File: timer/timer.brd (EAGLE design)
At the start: 100 x 80 mm, 8 parts, among them IC1 LM555N

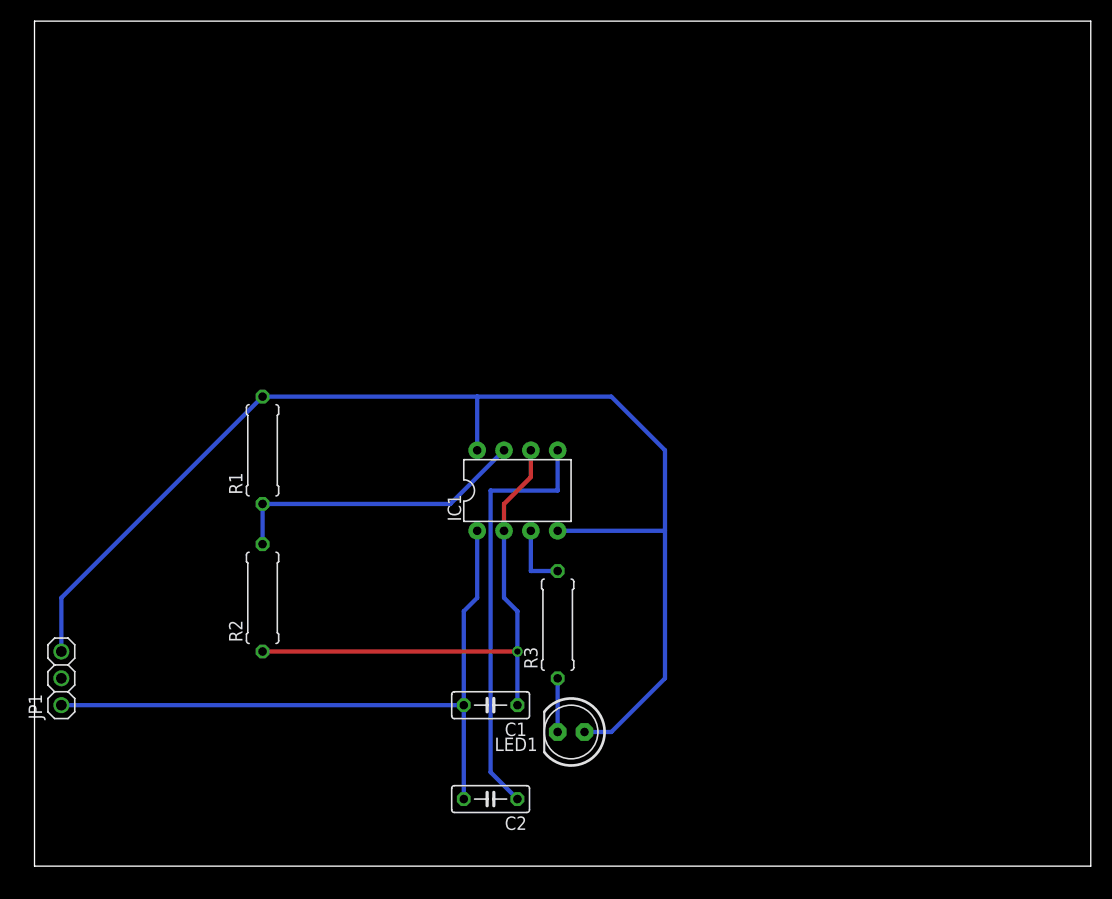
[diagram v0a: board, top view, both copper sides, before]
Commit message: add mounting holes
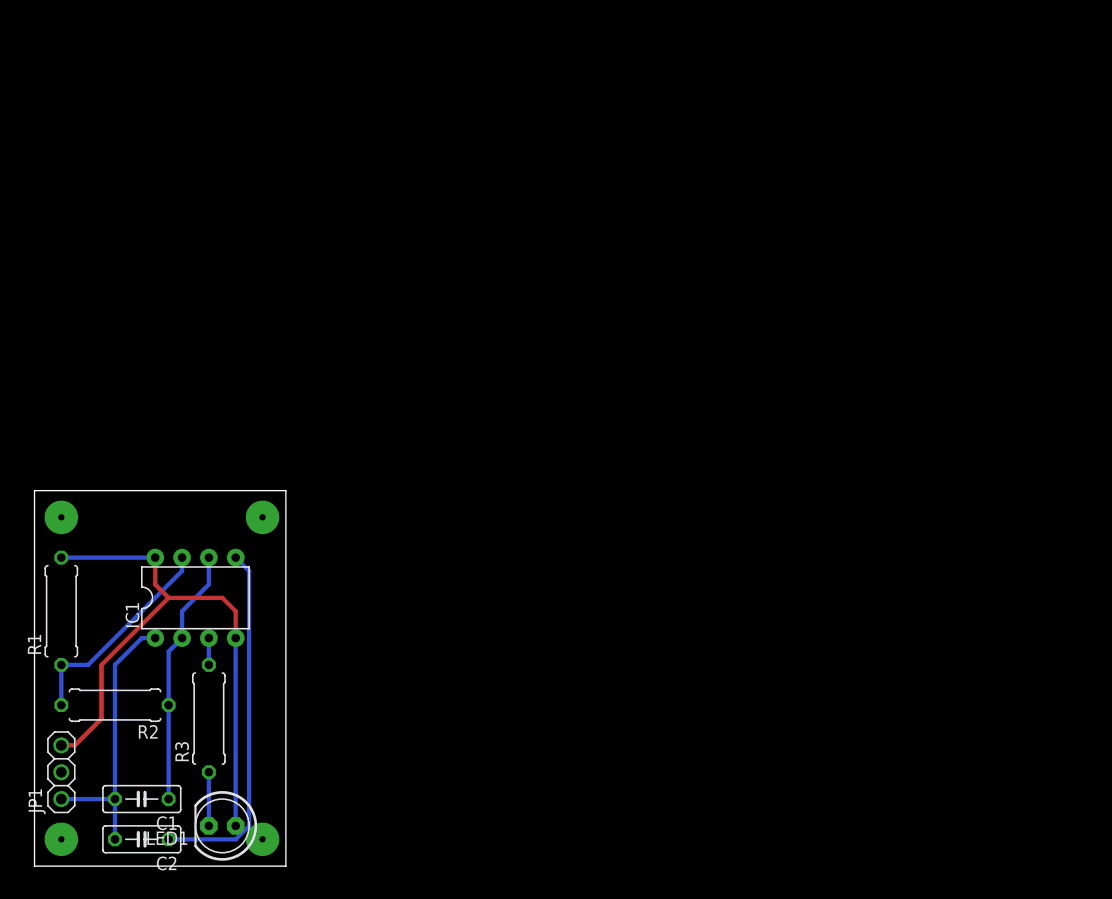
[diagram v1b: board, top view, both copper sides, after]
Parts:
- moved C1 34.2 mm to (10.2, 6.35)
- moved LED1 34.2 mm to (17.8, 3.81)
- moved R3 34.2 mm to (16.5, 14.0)
- moved C2 33.2 mm to (10.2, 2.54)
- moved IC1 32.1 mm to (15.2, 25.4)
- moved R1 24.4 mm to (2.54, 24.1)
- moved R2 17.3 mm to (7.62, 15.2), turned to 180 degrees
- moved JP1 8.89 mm to (2.54, 8.89)
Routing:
- net N$7: track 118.8 -> 59.3 mm
- net N$5: track 64.0 -> 26.5 mm
- net N$9: track 49.8 -> 24.4 mm, vias 1 -> 0
- net N$3: track 28.8 -> 20.2 mm
- net N$1: track 40.4 -> 34.1 mm
- net N$4: track 6.35 -> 2.54 mm
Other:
- board size 100 x 80 mm -> 23.8 x 35.5 mm
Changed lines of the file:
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@@
 <?xml version="1.0" encoding="utf-8"?>
 <!DOCTYPE eagle SYSTEM "eagle.dtd">
-<eagle version="6.2">
+<eagle version="6.3">
 <drawing>
 <settings>
@@
 <board>
 <plain>
-<wire x1="0" y1="0" x2="100" y2="0" width="0" layer="20"/>
-<wire x1="100" y1="0" x2="100" y2="80" width="0" layer="20"/>
-<wire x1="100" y1="80" x2="0" y2="80" width="0" layer="20"/>
-<wire x1="0" y1="80" x2="0" y2="0" width="0" layer="20"/>
+<wire x1="0" y1="0" x2="23.8" y2="0" width="0" layer="20"/>
+<wire x1="23.8" y1="0" x2="23.8" y2="35.55" width="0" layer="20"/>
+<wire x1="23.8" y1="35.55" x2="0" y2="35.55" width="0" layer="20"/>
+<wire x1="0" y1="35.55" x2="0" y2="0" width="0" layer="20"/>
 </plain>
 <attributes>
@@
 </class>
 </classes>
-<designrules>
+<designrules name="default">
 <description language="de">&lt;b&gt;EAGLE Design Rules&lt;/b&gt;
 &lt;p&gt;
@@
 </autorouter>
 <elements>
-<element name="IC1" library="adafruit" package="DIL08-ROUND" value="LM555N" x="45.72" y="35.56"/>
-<element name="R1" library="adafruit" package="0309/10" value="10k" x="21.59" y="39.37" rot="R90"/>
-<element name="R2" library="adafruit" package="0309/10" value="220k" x="21.59" y="25.4" rot="R90"/>
-<element name="R3" library="adafruit" package="0309/10" value="470" x="49.53" y="22.86" rot="R90"/>
-<element name="C2" library="adafruit" package="C050-025X075" value="0.1uf" x="43.18" y="6.35" rot="R180"/>
-<element name="C1" library="adafruit" package="C050-025X075" value="1uf" x="43.18" y="15.24" rot="R180"/>
-<element name="LED1" library="adafruit" package="LED5MM" value="" x="50.8" y="12.7" rot="R180"/>
-<element name="JP1" library="adafruit" package="1X03" value="" x="2.54" y="17.78" rot="R90"/>
+<element name="IC1" library="adafruit" package="DIL08-ROUND" value="LM555N" x="15.24" y="25.4"/>
+<element name="R1" library="adafruit" package="0309/10" value="10k" x="2.54" y="24.13" rot="R90"/>
+<element name="R2" library="adafruit" package="0309/10" value="220k" x="7.62" y="15.24" rot="R180"/>
+<element name="R3" library="adafruit" package="0309/10" value="470" x="16.51" y="13.97" rot="R90"/>
+<element name="C2" library="adafruit" package="C050-025X075" value="0.1uf" x="10.16" y="2.54" rot="R180"/>
+<element name="C1" library="adafruit" package="C050-025X075" value="1uf" x="10.16" y="6.35" rot="R180"/>
+<element name="LED1" library="adafruit" package="LED5MM" value="" x="17.78" y="3.81" rot="R180"/>
+<element name="JP1" library="adafruit" package="1X03" value="" x="2.54" y="8.89" rot="R90"/>
 </elements>
 <signals>
@@
 <contactref element="R2" pad="2"/>
 <contactref element="IC1" pad="7"/>
-<wire x1="21.59" y1="34.29" x2="21.59" y2="30.48" width="0.4064" layer="16"/>
-<wire x1="44.45" y1="39.37" x2="39.37" y2="34.29" width="0.4064" layer="16"/>
-<wire x1="39.37" y1="34.29" x2="21.59" y2="34.29" width="0.4064" layer="16"/>
+<wire x1="2.54" y1="19.05" x2="2.54" y2="15.24" width="0.4064" layer="16"/>
+<wire x1="13.97" y1="29.21" x2="13.97" y2="27.94" width="0.4064" layer="16"/>
+<wire x1="13.97" y1="27.94" x2="5.08" y2="19.05" width="0.4064" layer="16"/>
+<wire x1="5.08" y1="19.05" x2="2.54" y2="19.05" width="0.4064" layer="16"/>
 </signal>
 <signal name="N$5">
@@
 <contactref element="IC1" pad="1"/>
 <contactref element="C2" pad="2"/>
-<wire x1="40.64" y1="6.35" x2="40.64" y2="15.24" width="0.4064" layer="16"/>
-<wire x1="40.64" y1="15.24" x2="40.64" y2="24.13" width="0.4064" layer="16"/>
-<wire x1="40.64" y1="24.13" x2="41.91" y2="25.4" width="0.4064" layer="16"/>
-<wire x1="41.91" y1="25.4" x2="41.91" y2="31.75" width="0.4064" layer="16"/>
-<wire x1="2.54" y1="15.24" x2="40.64" y2="15.24" width="0.4064" layer="16"/>
+<wire x1="7.62" y1="2.54" x2="7.62" y2="6.35" width="0.4064" layer="16"/>
+<wire x1="2.54" y1="6.35" x2="7.62" y2="6.35" width="0.4064" layer="16"/>
+<wire x1="11.43" y1="21.59" x2="10.16" y2="21.59" width="0.4064" layer="16"/>
+<wire x1="10.16" y1="21.59" x2="7.62" y2="19.05" width="0.4064" layer="16"/>
+<wire x1="7.62" y1="19.05" x2="7.62" y2="6.35" width="0.4064" layer="16"/>
 </signal>
 <signal name="N$7">
@@
 <contactref element="IC1" pad="4"/>
 <contactref element="LED1" pad="A"/>
-<wire x1="21.59" y1="44.45" x2="41.91" y2="44.45" width="0.4064" layer="16"/>
-<wire x1="41.91" y1="44.45" x2="41.91" y2="39.37" width="0.4064" layer="16"/>
-<wire x1="54.61" y1="44.45" x2="41.91" y2="44.45" width="0.4064" layer="16"/>
-<wire x1="54.61" y1="44.45" x2="59.69" y2="39.37" width="0.4064" layer="16"/>
-<wire x1="59.69" y1="39.37" x2="59.69" y2="31.75" width="0.4064" layer="16"/>
-<wire x1="59.69" y1="31.75" x2="49.53" y2="31.75" width="0.4064" layer="16"/>
-<wire x1="52.07" y1="12.7" x2="54.61" y2="12.7" width="0.4064" layer="16"/>
-<wire x1="54.61" y1="12.7" x2="59.69" y2="17.78" width="0.4064" layer="16"/>
-<wire x1="59.69" y1="17.78" x2="59.69" y2="31.75" width="0.4064" layer="16"/>
-<wire x1="2.54" y1="20.32" x2="2.54" y2="25.4" width="0.4064" layer="16"/>
-<wire x1="2.54" y1="25.4" x2="21.59" y2="44.45" width="0.4064" layer="16"/>
+<wire x1="11.43" y1="29.21" x2="2.54" y2="29.21" width="0.4064" layer="16"/>
+<wire x1="11.43" y1="29.21" x2="11.43" y2="26.67" width="0.4064" layer="1"/>
+<wire x1="11.43" y1="26.67" x2="12.7" y2="25.4" width="0.4064" layer="1"/>
+<wire x1="12.7" y1="25.4" x2="17.78" y2="25.4" width="0.4064" layer="1"/>
+<wire x1="17.78" y1="25.4" x2="19.05" y2="24.13" width="0.4064" layer="1"/>
+<wire x1="19.05" y1="24.13" x2="19.05" y2="21.59" width="0.4064" layer="1"/>
+<wire x1="19.05" y1="3.81" x2="19.05" y2="21.59" width="0.4064" layer="16"/>
+<wire x1="2.54" y1="11.43" x2="3.81" y2="11.43" width="0.4064" layer="1"/>
+<wire x1="3.81" y1="11.43" x2="6.35" y2="13.97" width="0.4064" layer="1"/>
+<wire x1="6.35" y1="13.97" x2="6.35" y2="19.05" width="0.4064" layer="1"/>
+<wire x1="6.35" y1="19.05" x2="12.7" y2="25.4" width="0.4064" layer="1"/>
 </signal>
 <signal name="N$9">
@@
 <contactref element="IC1" pad="2"/>
 <contactref element="IC1" pad="6"/>
-<wire x1="45.72" y1="15.24" x2="45.72" y2="20.32" width="0.4064" layer="16"/>
-<wire x1="45.72" y1="20.32" x2="45.72" y2="24.13" width="0.4064" layer="16"/>
-<wire x1="45.72" y1="24.13" x2="44.45" y2="25.4" width="0.4064" layer="16"/>
-<wire x1="44.45" y1="25.4" x2="44.45" y2="31.75" width="0.4064" layer="16"/>
-<wire x1="21.59" y1="20.32" x2="45.72" y2="20.32" width="0.4064" layer="1"/>
-<via x="45.72" y="20.32" extent="1-16" drill="0.6" shape="square"/>
-<wire x1="44.45" y1="31.75" x2="44.45" y2="34.29" width="0.4064" layer="1"/>
-<wire x1="44.45" y1="34.29" x2="46.99" y2="36.83" width="0.4064" layer="1"/>
-<wire x1="46.99" y1="36.83" x2="46.99" y2="39.37" width="0.4064" layer="1"/>
+<wire x1="12.7" y1="15.24" x2="12.7" y2="6.35" width="0.4064" layer="16"/>
+<wire x1="13.97" y1="21.59" x2="12.7" y2="20.32" width="0.4064" layer="16"/>
+<wire x1="12.7" y1="20.32" x2="12.7" y2="15.24" width="0.4064" layer="16"/>
+<wire x1="16.51" y1="29.21" x2="16.51" y2="26.67" width="0.4064" layer="16"/>
+<wire x1="16.51" y1="26.67" x2="13.97" y2="24.13" width="0.4064" layer="16"/>
+<wire x1="13.97" y1="24.13" x2="13.97" y2="21.59" width="0.4064" layer="16"/>
 </signal>
 <signal name="N$1">
 <contactref element="IC1" pad="5"/>
 <contactref element="C2" pad="1"/>
-<wire x1="49.53" y1="39.37" x2="49.53" y2="35.56" width="0.4064" layer="16"/>
-<wire x1="49.53" y1="35.56" x2="43.18" y2="35.56" width="0.4064" layer="16"/>
-<wire x1="43.18" y1="35.56" x2="43.18" y2="8.89" width="0.4064" layer="16"/>
-<wire x1="43.18" y1="8.89" x2="45.72" y2="6.35" width="0.4064" layer="16"/>
+<wire x1="19.05" y1="29.21" x2="20.32" y2="27.94" width="0.4064" layer="16"/>
+<wire x1="20.32" y1="27.94" x2="20.32" y2="3.81" width="0.4064" layer="16"/>
+<wire x1="20.32" y1="3.81" x2="19.05" y2="2.54" width="0.4064" layer="16"/>
+<wire x1="19.05" y1="2.54" x2="12.7" y2="2.54" width="0.4064" layer="16"/>
 </signal>
 <signal name="N$2">
 <contactref element="LED1" pad="K"/>
 <contactref element="R3" pad="1"/>
-<wire x1="49.53" y1="12.7" x2="49.53" y2="17.78" width="0.4064" layer="16"/>
+<wire x1="16.51" y1="8.89" x2="16.51" y2="3.81" width="0.4064" layer="16"/>
 </signal>
 <signal name="N$4">
 <contactref element="R3" pad="2"/>
 <contactref element="IC1" pad="3"/>
-<wire x1="49.53" y1="27.94" x2="46.99" y2="27.94" width="0.4064" layer="16"/>
-<wire x1="46.99" y1="27.94" x2="46.99" y2="31.75" width="0.4064" layer="16"/>
+<wire x1="16.51" y1="21.59" x2="16.51" y2="19.05" width="0.4064" layer="16"/>
+</signal>
+<signal name="N$6">
+<via x="2.54" y="2.54" extent="1-16" drill="0.6" diameter="3.175" shape="square"/>
+</signal>
+<signal name="N$8">
+<via x="2.54" y="33.02" extent="1-16" drill="0.6" diameter="3.175" shape="square"/>
+</signal>
+<signal name="N$10">
+<via x="21.59" y="33.02" extent="1-16" drill="0.6" diameter="3.175" shape="square"/>
+</signal>
+<signal name="N$11">
+<via x="21.59" y="2.54" extent="1-16" drill="0.6" diameter="3.175" shape="square"/>
 </signal>
 </signals>

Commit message: improve packing
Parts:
- moved IC1 4.58 mm to (12.7, 29.2)
- moved R3 3.81 mm to (16.5, 17.8)
- moved LED1 3.81 mm to (17.8, 7.62)
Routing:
- net N$1: track 34.1 -> 38.9 mm
- net N$9: track 24.4 -> 28.2 mm
- net N$5: track 26.5 -> 28.5 mm
- net N$3: track 20.2 -> 21.5 mm
- net N$4: track 2.54 -> 3.59 mm
- net N$7: track 59.3 -> 58.6 mm
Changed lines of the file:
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@@
 </autorouter>
 <elements>
-<element name="IC1" library="adafruit" package="DIL08-ROUND" value="LM555N" x="15.24" y="25.4"/>
+<element name="IC1" library="adafruit" package="DIL08-ROUND" value="LM555N" x="12.7" y="29.21"/>
 <element name="R1" library="adafruit" package="0309/10" value="10k" x="2.54" y="24.13" rot="R90"/>
 <element name="R2" library="adafruit" package="0309/10" value="220k" x="7.62" y="15.24" rot="R180"/>
-<element name="R3" library="adafruit" package="0309/10" value="470" x="16.51" y="13.97" rot="R90"/>
+<element name="R3" library="adafruit" package="0309/10" value="470" x="16.51" y="17.78" rot="R90"/>
 <element name="C2" library="adafruit" package="C050-025X075" value="0.1uf" x="10.16" y="2.54" rot="R180"/>
 <element name="C1" library="adafruit" package="C050-025X075" value="1uf" x="10.16" y="6.35" rot="R180"/>
-<element name="LED1" library="adafruit" package="LED5MM" value="" x="17.78" y="3.81" rot="R180"/>
+<element name="LED1" library="adafruit" package="LED5MM" value="" x="17.78" y="7.62" rot="R180"/>
 <element name="JP1" library="adafruit" package="1X03" value="" x="2.54" y="8.89" rot="R90"/>
 </elements>
@@
 <contactref element="IC1" pad="7"/>
 <wire x1="2.54" y1="19.05" x2="2.54" y2="15.24" width="0.4064" layer="16"/>
-<wire x1="13.97" y1="29.21" x2="13.97" y2="27.94" width="0.4064" layer="16"/>
-<wire x1="13.97" y1="27.94" x2="5.08" y2="19.05" width="0.4064" layer="16"/>
-<wire x1="5.08" y1="19.05" x2="2.54" y2="19.05" width="0.4064" layer="16"/>
+<wire x1="11.43" y1="33.02" x2="11.43" y2="30.48" width="0.4064" layer="16"/>
+<wire x1="11.43" y1="30.48" x2="2.54" y2="21.59" width="0.4064" layer="16"/>
+<wire x1="2.54" y1="21.59" x2="2.54" y2="19.05" width="0.4064" layer="16"/>
 </signal>
 <signal name="N$5">
@@
 <wire x1="7.62" y1="2.54" x2="7.62" y2="6.35" width="0.4064" layer="16"/>
 <wire x1="2.54" y1="6.35" x2="7.62" y2="6.35" width="0.4064" layer="16"/>
-<wire x1="11.43" y1="21.59" x2="10.16" y2="21.59" width="0.4064" layer="16"/>
-<wire x1="10.16" y1="21.59" x2="7.62" y2="19.05" width="0.4064" layer="16"/>
-<wire x1="7.62" y1="19.05" x2="7.62" y2="6.35" width="0.4064" layer="16"/>
+<wire x1="8.89" y1="25.4" x2="7.62" y2="24.13" width="0.4064" layer="16"/>
+<wire x1="7.62" y1="24.13" x2="7.62" y2="6.35" width="0.4064" layer="16"/>
 </signal>
 <signal name="N$7">
@@
 <contactref element="IC1" pad="4"/>
 <contactref element="LED1" pad="A"/>
-<wire x1="11.43" y1="29.21" x2="2.54" y2="29.21" width="0.4064" layer="16"/>
-<wire x1="11.43" y1="29.21" x2="11.43" y2="26.67" width="0.4064" layer="1"/>
-<wire x1="11.43" y1="26.67" x2="12.7" y2="25.4" width="0.4064" layer="1"/>
-<wire x1="12.7" y1="25.4" x2="17.78" y2="25.4" width="0.4064" layer="1"/>
-<wire x1="17.78" y1="25.4" x2="19.05" y2="24.13" width="0.4064" layer="1"/>
-<wire x1="19.05" y1="24.13" x2="19.05" y2="21.59" width="0.4064" layer="1"/>
-<wire x1="19.05" y1="3.81" x2="19.05" y2="21.59" width="0.4064" layer="16"/>
-<wire x1="2.54" y1="11.43" x2="3.81" y2="11.43" width="0.4064" layer="1"/>
-<wire x1="3.81" y1="11.43" x2="6.35" y2="13.97" width="0.4064" layer="1"/>
-<wire x1="6.35" y1="13.97" x2="6.35" y2="19.05" width="0.4064" layer="1"/>
-<wire x1="6.35" y1="19.05" x2="12.7" y2="25.4" width="0.4064" layer="1"/>
+<wire x1="16.51" y1="25.4" x2="19.05" y2="22.86" width="0.4064" layer="16"/>
+<wire x1="19.05" y1="22.86" x2="19.05" y2="7.62" width="0.4064" layer="16"/>
+<wire x1="8.89" y1="33.02" x2="8.89" y2="30.48" width="0.4064" layer="1"/>
+<wire x1="8.89" y1="30.48" x2="10.16" y2="29.21" width="0.4064" layer="1"/>
+<wire x1="10.16" y1="29.21" x2="15.24" y2="29.21" width="0.4064" layer="1"/>
+<wire x1="15.24" y1="29.21" x2="16.51" y2="27.94" width="0.4064" layer="1"/>
+<wire x1="16.51" y1="27.94" x2="16.51" y2="25.4" width="0.4064" layer="1"/>
+<wire x1="2.54" y1="11.43" x2="15.24" y2="11.43" width="0.4064" layer="1"/>
+<wire x1="15.24" y1="11.43" x2="19.05" y2="7.62" width="0.4064" layer="1"/>
+<wire x1="2.54" y1="29.21" x2="5.08" y2="29.21" width="0.4064" layer="16"/>
+<wire x1="5.08" y1="29.21" x2="8.89" y2="33.02" width="0.4064" layer="16"/>
 </signal>
 <signal name="N$9">
@@
 <contactref element="IC1" pad="6"/>
 <wire x1="12.7" y1="15.24" x2="12.7" y2="6.35" width="0.4064" layer="16"/>
-<wire x1="13.97" y1="21.59" x2="12.7" y2="20.32" width="0.4064" layer="16"/>
-<wire x1="12.7" y1="20.32" x2="12.7" y2="15.24" width="0.4064" layer="16"/>
-<wire x1="16.51" y1="29.21" x2="16.51" y2="26.67" width="0.4064" layer="16"/>
-<wire x1="16.51" y1="26.67" x2="13.97" y2="24.13" width="0.4064" layer="16"/>
-<wire x1="13.97" y1="24.13" x2="13.97" y2="21.59" width="0.4064" layer="16"/>
+<wire x1="12.7" y1="15.24" x2="12.7" y2="24.13" width="0.4064" layer="16"/>
+<wire x1="12.7" y1="24.13" x2="11.43" y2="25.4" width="0.4064" layer="16"/>
+<wire x1="13.97" y1="33.02" x2="13.97" y2="30.48" width="0.4064" layer="16"/>
+<wire x1="13.97" y1="30.48" x2="11.43" y2="27.94" width="0.4064" layer="16"/>
+<wire x1="11.43" y1="27.94" x2="11.43" y2="25.4" width="0.4064" layer="16"/>
 </signal>
 <signal name="N$1">
 <contactref element="IC1" pad="5"/>
 <contactref element="C2" pad="1"/>
-<wire x1="19.05" y1="29.21" x2="20.32" y2="27.94" width="0.4064" layer="16"/>
-<wire x1="20.32" y1="27.94" x2="20.32" y2="3.81" width="0.4064" layer="16"/>
+<wire x1="16.51" y1="33.02" x2="20.32" y2="29.21" width="0.4064" layer="16"/>
+<wire x1="20.32" y1="29.21" x2="20.32" y2="3.81" width="0.4064" layer="16"/>
 <wire x1="20.32" y1="3.81" x2="19.05" y2="2.54" width="0.4064" layer="16"/>
 <wire x1="19.05" y1="2.54" x2="12.7" y2="2.54" width="0.4064" layer="16"/>
@@
 <contactref element="LED1" pad="K"/>
 <contactref element="R3" pad="1"/>
-<wire x1="16.51" y1="8.89" x2="16.51" y2="3.81" width="0.4064" layer="16"/>
+<wire x1="16.51" y1="12.7" x2="16.51" y2="7.62" width="0.4064" layer="16"/>
 </signal>
 <signal name="N$4">
 <contactref element="R3" pad="2"/>
 <contactref element="IC1" pad="3"/>
-<wire x1="16.51" y1="21.59" x2="16.51" y2="19.05" width="0.4064" layer="16"/>
+<wire x1="13.97" y1="25.4" x2="16.51" y2="22.86" width="0.4064" layer="16"/>
 </signal>
 <signal name="N$6">
